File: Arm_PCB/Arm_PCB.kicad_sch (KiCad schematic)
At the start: 29 parts, among them J1 Conn_02x04_Counter_Clockwise, J10 Conn_02x02_Counter_Clockwise, J11 Conn_02x04_Counter_Clockwise, J12 Screw_Terminal_01x02, J13 Screw_Terminal_01x02, J14 Screw_Terminal_01x02, J15 Screw_Terminal_01x02, J16 Screw_Terminal_01x02, J17 Screw_Terminal_01x02, J18 Screw_Terminal_01x02, J2 Conn_02x04_Counter_Clockwise, J3 Conn_02x04_Counter_Clockwise, J4 Conn_02x04_Counter_Clockwise, J5 Conn_02x05_Counter_Clockwise, J6 Conn_02x07_Counter_Clockwise, J7 Conn_02x03_Counter_Clockwise, J8 Conn_02x02_Counter_Clockwise, J9 Conn_02x04_Counter_Clockwise, SW1 SW_Push, SW2 SW_Push, SW3 SW_Push, SW4 SW_Push

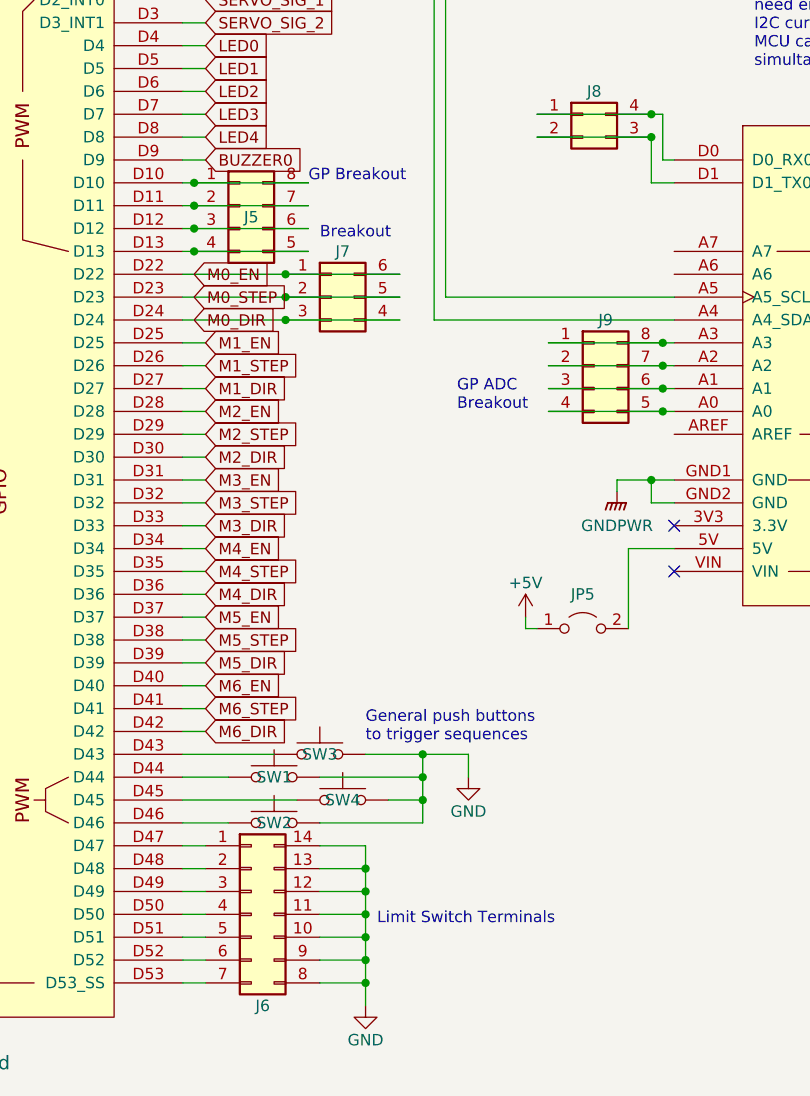
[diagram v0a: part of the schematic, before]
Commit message: Add spotlight and resistors on limit switches
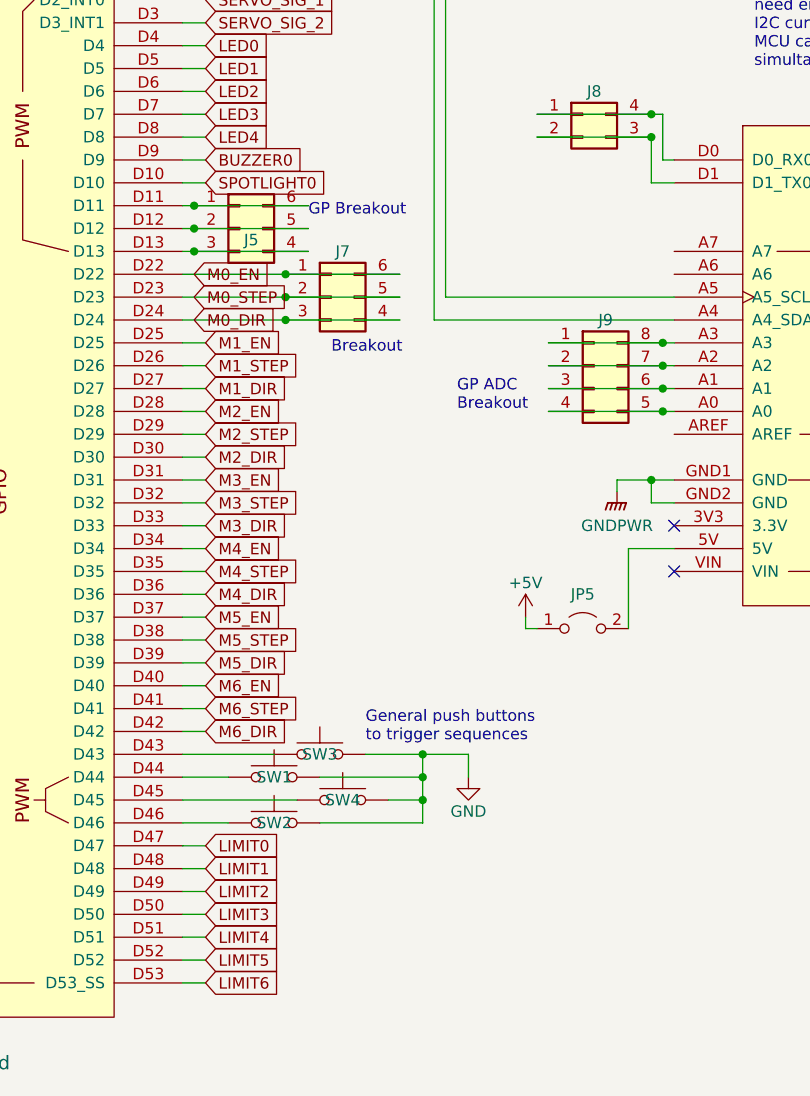
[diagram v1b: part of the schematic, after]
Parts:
- removed J6: Conn_02x07_Counter_Clockwise, symbol Connector_Generic:Conn_02x07_Counter_Clockwise
- J5: symbol Connector_Generic:Conn_02x04_Counter_Clockwise -> Connector_Generic:Conn_02x03_Counter_Clockwise
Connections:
- net at J5.4 (Pin_4), XA1.D13: now also J5.3 (Pin_3); no longer J5.5 (Pin_5)
- net LIMIT0: now reaches XA1.D47
- net LIMIT1: now reaches XA1.D48
- net LIMIT2: now reaches XA1.D49
- net LIMIT3: now reaches XA1.D50
- net LIMIT4: now reaches XA1.D51
- net LIMIT5: now reaches XA1.D52
- net LIMIT6: now reaches XA1.D53 (D53_SS)
- new net: J5.1 (Pin_1), J5.6 (Pin_6), XA1.D11
- new net: J5.2 (Pin_2), J5.5 (Pin_5), XA1.D12
- new net SPOTLIGHT0: XA1.D10
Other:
- note removed: "Limit Switch Terminals"

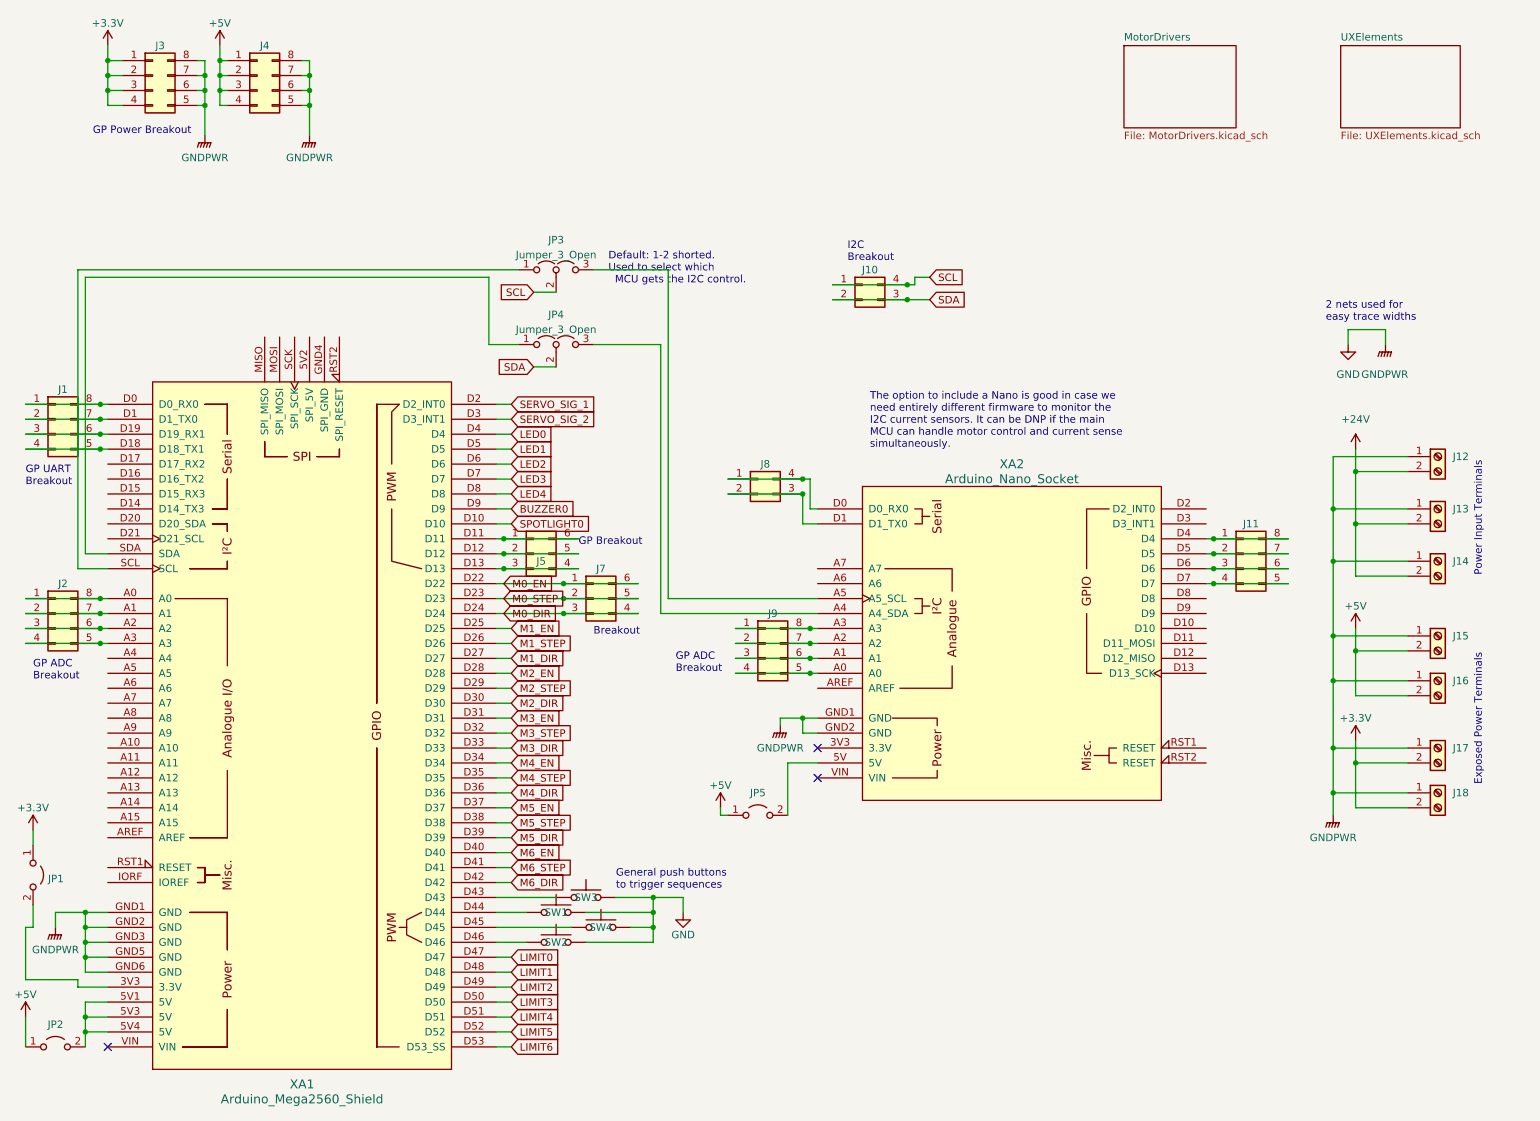
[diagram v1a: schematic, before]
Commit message: Added a basic footprint for the PCB
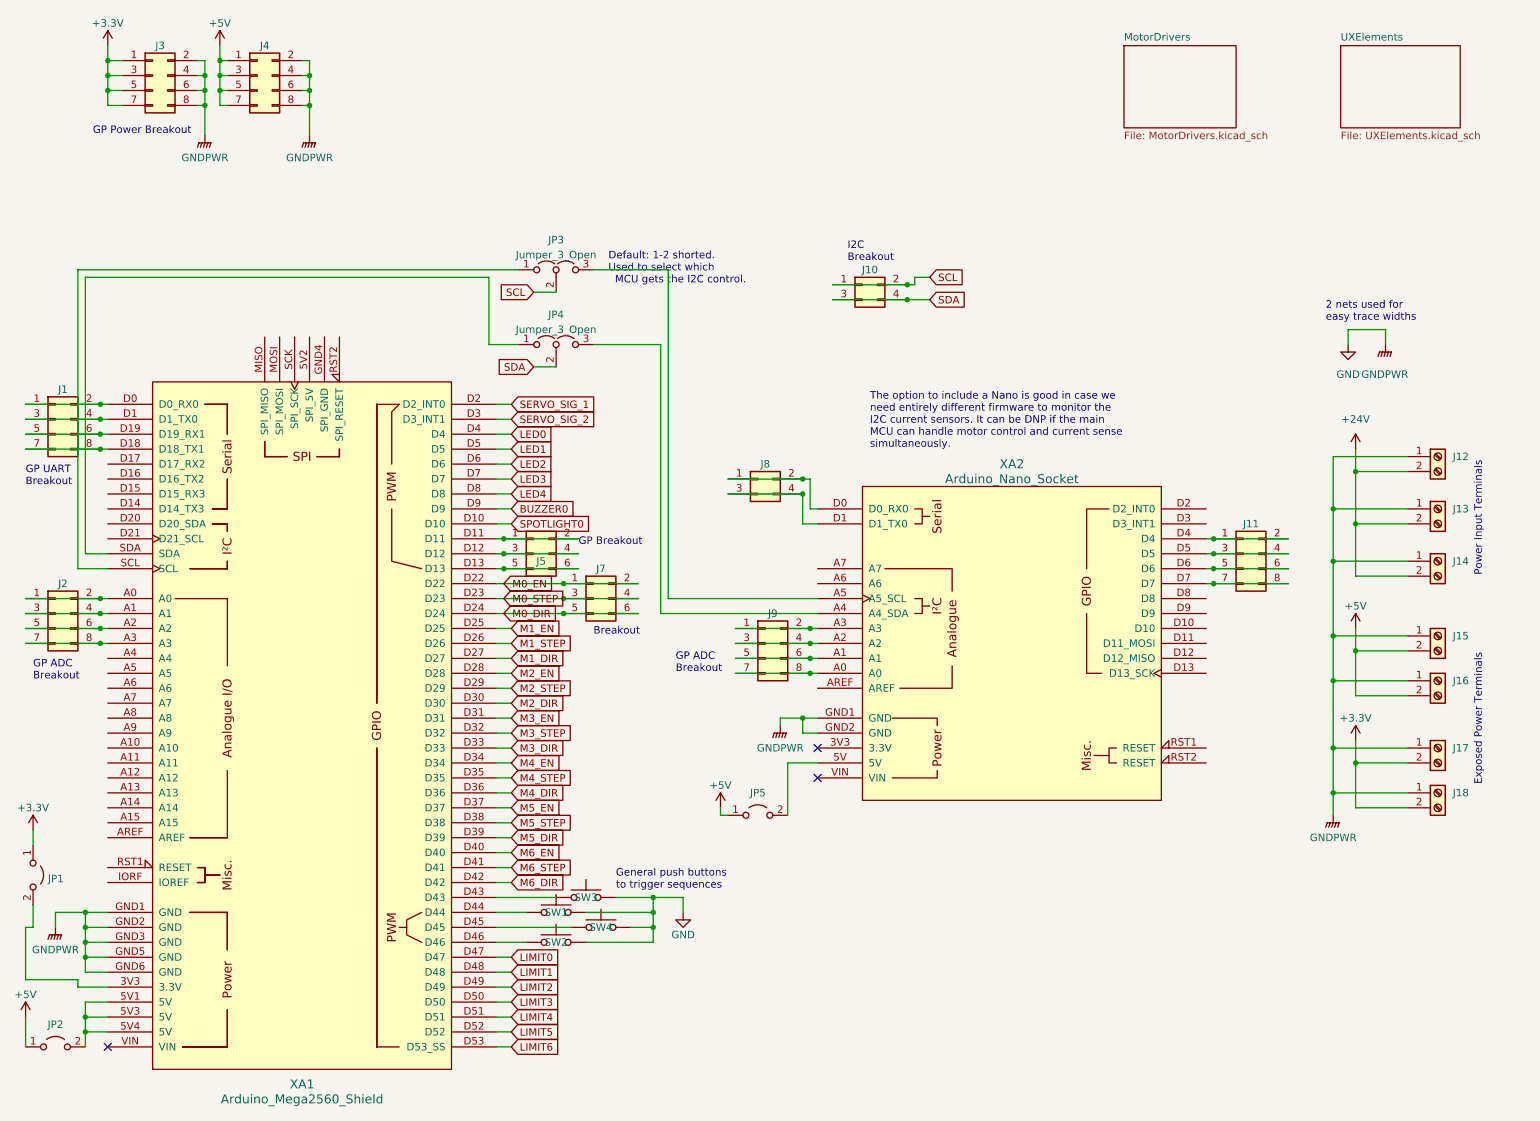
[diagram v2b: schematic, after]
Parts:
- J1, J11, J2, J3, J4, J9: footprint (none) -> Connector_PinHeader_2.54mm:PinHeader_2x04_P2.54mm_Vertical; symbol Connector_Generic:Conn_02x04_Counter_Clockwise -> Connector_Generic:Conn_02x04_Odd_Even
- J10, J8: footprint (none) -> Connector_PinHeader_2.54mm:PinHeader_2x02_P2.54mm_Vertical; symbol Connector_Generic:Conn_02x02_Counter_Clockwise -> Connector_Generic:Conn_02x02_Odd_Even
- J12, J13, J14, J15, J16, J17, J18: footprint (none) -> TerminalBlock:TerminalBlock_bornier-2_P5.08mm
- J5: value Conn_02x05_Counter_Clockwise -> Conn_02x03_Counter_Clockwise; footprint (none) -> Connector_PinHeader_2.54mm:PinHeader_2x03_P2.54mm_Vertical; symbol Connector_Generic:Conn_02x03_Counter_Clockwise -> Connector_Generic:Conn_02x03_Odd_Even
- J7: footprint (none) -> Connector_PinHeader_2.54mm:PinHeader_2x03_P2.54mm_Vertical; symbol Connector_Generic:Conn_02x03_Counter_Clockwise -> Connector_Generic:Conn_02x03_Odd_Even
- JP1, JP2, JP5: footprint (none) -> Connector_PinHeader_2.54mm:PinHeader_1x02_P2.54mm_Vertical
- JP3, JP4: footprint (none) -> Connector_PinHeader_2.54mm:PinHeader_1x03_P2.54mm_Vertical
- SW1, SW2, SW3, SW4: footprint (none) -> Button_Switch_THT:SW_PUSH_6mm
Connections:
- net +3.3V: now also J3.5 (Pin_5), J3.7 (Pin_7); no longer J3.2 (Pin_2), J3.4 (Pin_4)
- net +5V: now also J4.5 (Pin_5), J4.7 (Pin_7); no longer J4.2 (Pin_2), J4.4 (Pin_4)
- net GND: now also J3.2 (Pin_2), J3.4 (Pin_4), J4.2 (Pin_2), J4.4 (Pin_4); no longer J3.5 (Pin_5), J3.7 (Pin_7), J4.5 (Pin_5), J4.7 (Pin_7)
- net M0_DIR: now also J7.5 (Pin_5), J7.6 (Pin_6); no longer J7.3 (Pin_3), J7.4 (Pin_4)
- net M0_EN: now also J7.2 (Pin_2); no longer J7.6 (Pin_6)
- net M0_STEP: now also J7.3 (Pin_3), J7.4 (Pin_4); no longer J7.2 (Pin_2), J7.5 (Pin_5)
- net SCL: now also J10.2 (Pin_2); no longer J10.4 (Pin_4)
- net SDA: now also J10.4 (Pin_4); no longer J10.2 (Pin_2)
- net at J2.1 (Pin_1), XA1.A0: now also J2.2 (Pin_2); no longer J2.8 (Pin_8)
- net at J2.6 (Pin_6), XA1.A2: now also J2.5 (Pin_5); no longer J2.3 (Pin_3)
- net at J1.1 (Pin_1), XA1.D0 (D0_RX0): now also J1.2 (Pin_2); no longer J1.8 (Pin_8)
- net at J1.6 (Pin_6), XA1.D19 (D19_RX1): now also J1.5 (Pin_5); no longer J1.3 (Pin_3)
- net at J5.1 (Pin_1), XA1.D11: now also J5.2 (Pin_2); no longer J5.6 (Pin_6)
- net at J5.3 (Pin_3), J5.4 (Pin_4): now also XA1.D12; no longer XA1.D13
- net at J11.1 (Pin_1), XA2.D4: now also J11.2 (Pin_2); no longer J11.8 (Pin_8)
- net at J11.6 (Pin_6), XA2.D6: now also J11.5 (Pin_5); no longer J11.3 (Pin_3)
- net at J8.1 (Pin_1), XA2.D0 (D0_RX0): now also J8.2 (Pin_2); no longer J8.4 (Pin_4)
- net at J8.3 (Pin_3), XA2.D1 (D1_TX0): now also J8.4 (Pin_4); no longer J8.2 (Pin_2)
- net at J9.6 (Pin_6), XA2.A1: now also J9.5 (Pin_5); no longer J9.3 (Pin_3)
- net at J9.1 (Pin_1), XA2.A3: now also J9.2 (Pin_2); no longer J9.8 (Pin_8)
- new net: J2.3 (Pin_3), J2.4 (Pin_4), XA1.A1
- new net: J2.7 (Pin_7), J2.8 (Pin_8), XA1.A3
- new net: J1.3 (Pin_3), J1.4 (Pin_4), XA1.D1 (D1_TX0)
- new net: J1.7 (Pin_7), J1.8 (Pin_8), XA1.D18 (D18_TX1)
- new net: J5.5 (Pin_5), J5.6 (Pin_6), XA1.D13
- new net: J11.3 (Pin_3), J11.4 (Pin_4), XA2.D5
- new net: J11.7 (Pin_7), J11.8 (Pin_8), XA2.D7
- new net: J9.7 (Pin_7), J9.8 (Pin_8), XA2.A0
- new net: J9.3 (Pin_3), J9.4 (Pin_4), XA2.A2
